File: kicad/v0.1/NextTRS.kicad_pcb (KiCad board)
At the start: 2 copper layers, 62 parts, among them J1 TRS-80 M3 Pin Header, J10 DB15_Female_HighDensity, J2 TRS-80 M1 Pin Connector, J3 TRS-80 M3 Edge Connector, J4 TRS-80 M1 Edge Connector, J5 AudioJack3, J6 Mini-DIN-6, J7 USB_B_Micro, J8 SD_Card, J9 Programmer, Q1 2N7002, Q2 2N7002, Q3 2N7002, Q4 MMBT3904, Q5 MMBT3904, SW1 SW_DIP_x04, SW2 SW_Push, SW3 SW_Push, SW4 ESP_RESET, SW5 PTRS_RESET, U1 ESP32-WROVER-B, U2 74LVC245, U3 74LVC245, U4 MCP43x1, U5 74LVC245, U6 74LVC245, U7 74LVC245

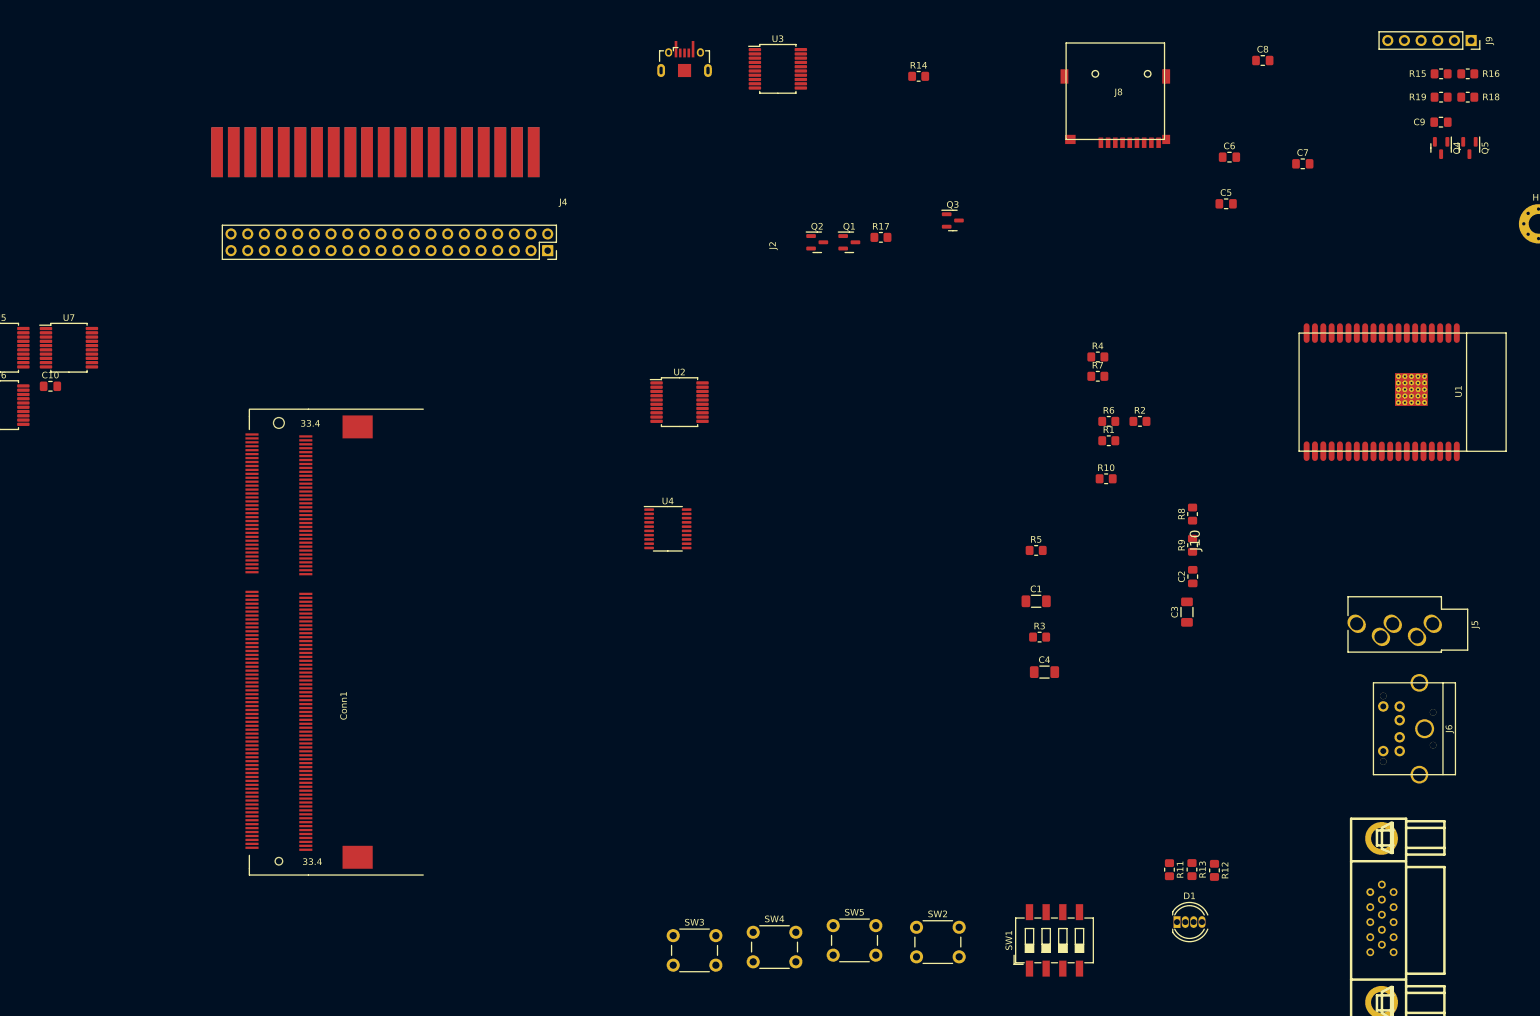
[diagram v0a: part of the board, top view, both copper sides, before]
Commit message: Do not use Bank 4 (1.5V)
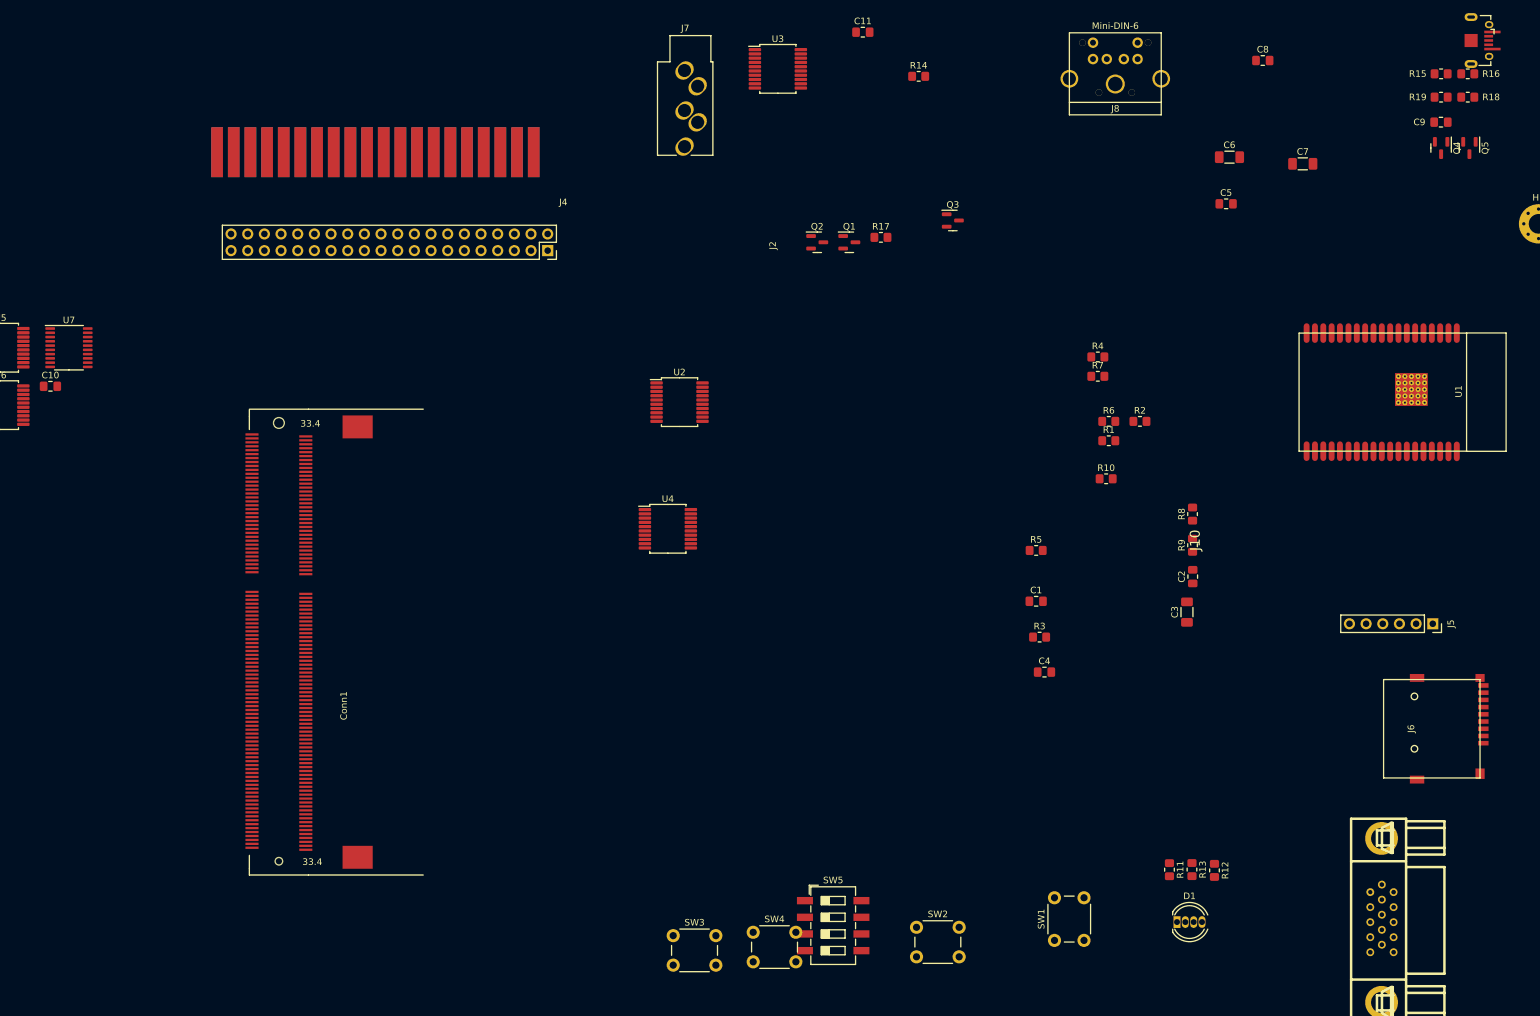
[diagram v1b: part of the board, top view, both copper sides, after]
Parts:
- added C11: 0.1uF, Capacitor_SMD:C_0805_2012Metric_Pad1.18x1.45mm_HandSolder, F.Cu at (170.4, 16.0)
- C1: value 1U -> 0.1uF; footprint Capacitor_SMD:C_1206_3216Metric_Pad1.33x1.80mm_HandSolder -> Capacitor_SMD:C_0805_2012Metric_Pad1.18x1.45mm_HandSolder
- C2: value 100N -> 0.1uF
- C3: value 10U -> 1U
- C4: value 10U -> 100N; footprint Capacitor_SMD:C_1206_3216Metric_Pad1.33x1.80mm_HandSolder -> Capacitor_SMD:C_0805_2012Metric_Pad1.18x1.45mm_HandSolder
- C6: value 0.1uF -> 10U; footprint Capacitor_SMD:C_0805_2012Metric_Pad1.18x1.45mm_HandSolder -> Capacitor_SMD:C_1206_3216Metric_Pad1.33x1.80mm_HandSolder
- C7: value 100N -> 10U; footprint Capacitor_SMD:C_0805_2012Metric_Pad1.18x1.45mm_HandSolder -> Capacitor_SMD:C_1206_3216Metric_Pad1.33x1.80mm_HandSolder
- C8: value 0.1uF -> 100N
- J5: value AudioJack3 -> Programmer; footprint PocketTRS_Connectors:Jack_3.5mm_CUI_SJ1-3535NG_Horizontal_CircularHoles -> Connector_PinSocket_2.54mm:PinSocket_1x06_P2.54mm_Vertical
- J6: value Mini-DIN-6 -> SD_Card; footprint PocketTRS_Connectors:minidin_6_ps2_pcb_mount -> PocketTRS_Connectors:TFP09-2-12B
- J7: value USB_B_Micro -> AudioJack3; footprint PocketTRS_Connectors:USBmicro-B -> PocketTRS_Connectors:Jack_3.5mm_CUI_SJ1-3535NG_Horizontal_CircularHoles
- J8: value SD_Card -> Mini-DIN-6; footprint PocketTRS_Connectors:TFP09-2-12B -> PocketTRS_Connectors:minidin_6_ps2_pcb_mount
- J9: value Programmer -> USB_B_Micro; footprint Connector_PinSocket_2.54mm:PinSocket_1x06_P2.54mm_Vertical -> PocketTRS_Connectors:USBmicro-B
- R1, R2: value 4K7 -> 100
- R10: value 10K -> 4K7
- R11: value 100 -> 4K7
- R12: value 100 -> 270R
- R13: value 100 -> 150R
- R15, R16: value 12K -> 4K7
- R17, R18: value 4K7 -> 2K
- R3: value 270R -> 100
- R4: value 150R -> 10K
- R5: value 2K -> 10K
- R6: value 2K -> 12K
- R7: value 10K -> 12K
- SW1: value SW_DIP_x04 -> SW_Push; footprint Button_Switch_SMD:SW_DIP_SPSTx04_Slide_6.7x11.72mm_W8.61mm_P2.54mm_LowProfile -> Button_Switch_THT:SW_PUSH_6mm
- SW2: value SW_Push -> ESP_RESET
- SW3: value SW_Push -> PTRS_RESET
- SW4: value ESP_RESET -> SW_Push
- SW5: value PTRS_RESET -> SW_DIP_x04; footprint Button_Switch_THT:SW_PUSH_6mm -> Button_Switch_SMD:SW_DIP_SPSTx04_Slide_6.7x11.72mm_W8.61mm_P2.54mm_LowProfile
- U4: value MCP43x1 -> 74LVC245; footprint Package_SO:TSSOP-20_4.4x6.5mm_P0.65mm -> Package_SO:SSOP-20_5.3x7.2mm_P0.65mm
- U7: value 74LVC245 -> MCP43x1; footprint Package_SO:SSOP-20_5.3x7.2mm_P0.65mm -> Package_SO:TSSOP-20_4.4x6.5mm_P0.65mm
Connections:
- C1 pad 1: CASS_IN -> GND
- C1 pad 2: GND -> +3V3
- C2 pad 1: Net-(C2-Pad1) -> GND
- C2 pad 2: GND -> +3V3
- C3 pad 1: Net-(C3-Pad1) -> CASS_IN
- C3 pad 2: CASS_IN -> GND
- C4 pad 2: Net-(C2-Pad1) -> GND
- C6 pad 1: GND -> Net-(C6-Pad1)
- C6 pad 2: +3V3 -> CASS_IN
- C7 pad 1: ESP_RESET -> Net-(C7-Pad1)
- C7 pad 2: GND -> Net-(C4-Pad1)
- C8 pad 1: GND -> ESP_RESET
- C8 pad 2: +3V3 -> GND
- Conn1 pad 158: INT_OUT_N -> unconnected-(Conn1-Pad158)
- Conn1 pad 160: WAIT_OUT_N -> unconnected-(Conn1-Pad160)
- Conn1 pad 180: unconnected-(Conn1-Pad180) -> WAIT_OUT_N
- Conn1 pad 182: unconnected-(Conn1-Pad182) -> INT_OUT_N
- J6 pad 1: PS2_DATA -> Net-(J6-Pad1)
- J6 pad 2: unconnected-(J6-Pad2) -> CS_SD
- J6 pad 3: GND -> MOSI
- J6 pad 4: +5V -> +3.3V
- J6 pad 5: PS2_CLK -> SCK
- J6 pad 6: unconnected-(J6-Pad6) -> GND
- J8 pad 1: Net-(J8-Pad1) -> PS2_DATA
- J8 pad 2: CS_SD -> unconnected-(J8-Pad2)
- J8 pad 3: MOSI -> GND
- J8 pad 4: +3.3V -> +5V
- J8 pad 5: SCK -> PS2_CLK
- J8 pad 6: GND -> unconnected-(J8-Pad6)
- J9 pad 1: Net-(J9-Pad1) -> +5V
- J9 pad 2: Net-(J9-Pad2) -> unconnected-(J9-Pad2)
- J9 pad 3: TXD0 -> unconnected-(J9-Pad3)
- J9 pad 4: RXD0 -> unconnected-(J9-Pad4)
- J9 pad 5: +5V -> GND
- Q4 pad 2: Net-(J9-Pad1) -> Net-(J5-Pad1)
- Q5 pad 2: Net-(J9-Pad2) -> Net-(J5-Pad2)
- R1 pad 1: +3.3V -> LED_RED
- R1 pad 2: CASS_IN -> Net-(D1-Pad1)
- R10 pad 2: Net-(J8-Pad1) -> CASS_IN
- R11 pad 1: LED_RED -> CASS_IN
- R11 pad 2: Net-(D1-Pad1) -> GND
- R12 pad 1: LED_GREEN -> Net-(C4-Pad1)
- R12 pad 2: Net-(D1-Pad4) -> CASS_OUT
- R13 pad 1: LED_BLUE -> Net-(C4-Pad1)
- R13 pad 2: Net-(D1-Pad3) -> GND
- R14 pad 1: +3.3V -> +3V3
- R14 pad 2: BUTTON -> I00
- R15 pad 1: Net-(Q4-Pad1) -> +3V3
- R15 pad 2: Net-(J9-Pad2) -> ESP_RESET
- R16 pad 1: Net-(Q5-Pad1) -> +3V3
- R16 pad 2: Net-(J9-Pad1) -> PTRS_RESET
- R17 pad 1: +3V3 -> PS2_CLK
- R17 pad 2: PTRS_RESET -> +3.3V
- R18 pad 1: +3V3 -> PS2_DATA
- R18 pad 2: I00 -> +3.3V
- R19 pad 1: +3V3 -> +3.3V
- R19 pad 2: ESP_RESET -> BUTTON
- R2 pad 1: CASS_IN -> LED_GREEN
- R2 pad 2: GND -> Net-(D1-Pad4)
- R3 pad 1: Net-(C2-Pad1) -> LED_BLUE
- R3 pad 2: CASS_OUT -> Net-(D1-Pad3)
- R4 pad 1: Net-(C2-Pad1) -> +3.3V
- R4 pad 2: GND -> MOSI
- R5 pad 1: PS2_CLK -> +3.3V
- R5 pad 2: +3.3V -> Net-(J6-Pad8)
- R6 pad 1: PS2_DATA -> Net-(Q4-Pad1)
- R6 pad 2: +3.3V -> Net-(J5-Pad2)
- R7 pad 1: +3.3V -> Net-(Q5-Pad1)
- R7 pad 2: MOSI -> Net-(J5-Pad1)
- R8 pad 2: Net-(J8-Pad8) -> CS_SD
- R9 pad 2: CS_SD -> Net-(J6-Pad1)
- SW1 pad 2: GND -> BUTTON
- SW2 pad 1: GND -> ESP_RESET
- SW2 pad 2: BUTTON -> GND
- SW3 pad 2: BUTTON -> PTRS_RESET
- SW4 pad 1: ESP_RESET -> GND
- SW4 pad 2: GND -> BUTTON
- SW5 pad 2: PTRS_RESET -> GND
- U4 pad 1: unconnected-(U4-Pad1) -> ABUS_DIR
- U4 pad 10: VGA_GREEN -> GND
- U4 pad 11: VGA_RED -> _A15
- U4 pad 12: POT_VGA_RED -> _A14
- U4 pad 13: GND -> _A13
- U4 pad 14: unconnected-(U4-Pad14) -> _A12
- U4 pad 15: unconnected-(U4-Pad15) -> _A11
- U4 pad 16: MISO -> _A10
- U4 pad 17: +3V3 -> _A9
- U4 pad 18: GND -> _A8
- U4 pad 19: POT_VGA_BLUE -> ABUS_EN
- U4 pad 2: unconnected-(U4-Pad2) -> A8
- U4 pad 20: VGA_BLUE -> +3V3
- U4 pad 3: unconnected-(U4-Pad3) -> A9
- U4 pad 4: CS43x1 -> A10
- U4 pad 5: SCK -> A11
- U4 pad 6: MOSI -> A12
- U4 pad 7: GND -> A13
- U4 pad 8: GND -> A14
- U4 pad 9: POT_VGA_GREEN -> A15
- U5 pad 1: ABUS_DIR -> +3V3
- U5 pad 11: _A15 -> unconnected-(U5-Pad11)
- U5 pad 12: _A14 -> unconnected-(U5-Pad12)
- U5 pad 13: _A13 -> unconnected-(U5-Pad13)
- U5 pad 14: _A12 -> unconnected-(U5-Pad14)
- U5 pad 15: _A11 -> unconnected-(U5-Pad15)
- U5 pad 16: _A10 -> INT_N
- U5 pad 17: _A9 -> WAIT_N
- U5 pad 18: _A8 -> EXTIOSEL_N
- U5 pad 19: ABUS_EN -> CTRL1_EN
- U5 pad 2: A8 -> EXTIOSEL_OUT_N
- U5 pad 3: A9 -> WAIT_OUT_N
- U5 pad 4: A10 -> INT_OUT_N
- U5 pad 5: A11 -> unconnected-(U5-Pad5)
- U5 pad 6: A12 -> unconnected-(U5-Pad6)
- U5 pad 7: A13 -> unconnected-(U5-Pad7)
- U5 pad 8: A14 -> unconnected-(U5-Pad8)
- U5 pad 9: A15 -> unconnected-(U5-Pad9)
- U6 pad 1: +3V3 -> DBUS_DIR
- U6 pad 11: unconnected-(U6-Pad11) -> _D7
- U6 pad 12: unconnected-(U6-Pad12) -> _D6
- U6 pad 13: unconnected-(U6-Pad13) -> _D5
- U6 pad 14: unconnected-(U6-Pad14) -> _D4
- U6 pad 15: unconnected-(U6-Pad15) -> _D3
- U6 pad 16: INT_N -> _D2
- U6 pad 17: WAIT_N -> _D1
- U6 pad 18: EXTIOSEL_N -> _D0
- U6 pad 19: CTRL1_EN -> DBUS_EN
- U6 pad 2: EXTIOSEL_OUT_N -> D0
- U6 pad 3: WAIT_OUT_N -> D1
- U6 pad 4: INT_OUT_N -> D2
- U6 pad 5: unconnected-(U6-Pad5) -> D3
- U6 pad 6: unconnected-(U6-Pad6) -> D4
- U6 pad 7: unconnected-(U6-Pad7) -> D5
- U6 pad 8: unconnected-(U6-Pad8) -> D6
- U6 pad 9: unconnected-(U6-Pad9) -> D7
- U7 pad 1: DBUS_DIR -> unconnected-(U7-Pad1)
- U7 pad 10: GND -> VGA_GREEN
- U7 pad 11: _D7 -> VGA_RED
- U7 pad 12: _D6 -> POT_VGA_RED
- U7 pad 13: _D5 -> GND
- U7 pad 14: _D4 -> unconnected-(U7-Pad14)
- U7 pad 15: _D3 -> unconnected-(U7-Pad15)
- U7 pad 16: _D2 -> MISO
- U7 pad 17: _D1 -> +3V3
- U7 pad 18: _D0 -> GND
- U7 pad 19: DBUS_EN -> POT_VGA_BLUE
- U7 pad 2: D0 -> unconnected-(U7-Pad2)
- U7 pad 20: +3V3 -> VGA_BLUE
- U7 pad 3: D1 -> unconnected-(U7-Pad3)
- U7 pad 4: D2 -> CS43x1
- U7 pad 5: D3 -> SCK
- U7 pad 6: D4 -> MOSI
- U7 pad 7: D5 -> GND
- U7 pad 8: D6 -> GND
- U7 pad 9: D7 -> POT_VGA_GREEN
